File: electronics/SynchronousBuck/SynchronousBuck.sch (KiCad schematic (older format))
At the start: 58 parts, among them J101 Conn_01x02, J102 Conn_01x04_Male, J103 Conn_01x02, J104 Conn_01x02, Q101 BSC070N10NS5, Q102 BSC067N06LS3G, U101 LM5116MH

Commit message: Updated layout and schematic. Added zener diodes to protect output of measurements
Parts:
- removed R102, R109, R110: 1k2, Resistor_SMD:R_0603_1608Metric, symbol Device:R_Small
- added D102, D103: 5V1, Diode_SMD:D_SOD-123, symbol Device:D_Zener
- added R120: 24k, Resistor_SMD:R_0603_1608Metric, symbol Device:R_Small
- C101, C111: symbol Device:C -> Device:C_Small
- R101: value 24k -> 18k
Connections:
- net GND: now also C116.2, C117.2, C120.2, C121.2, R111.1, D102.2 (A), D103.2 (A); no longer C116.1, C117.1, C120.1, C121.1, R111.2
- net VCC: now also C120.1, C121.1, R101.2; no longer C120.2, C121.2, R101.1
- net VOUT: now also C116.1, C117.1, R120.1; no longer C116.2, C117.2
- net at U101.2 (UVLO): now also R101.1, R111.2; no longer R111.1
- net at J102.1 (Pin_1), R121.1, R123.2: now also D103.1 (K), R120.2
- net at J102.4 (Pin_4), R117.2, R118.1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: now also D102.1 (K)
- no-connect marks 1 -> 0
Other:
- note added: "Ethernet over power connection"
- note added: "Vin 20-50V"
- note added: "Vout set 14.5V\n"
- note removed: "Vin 30-50V"
- moved on the sheet: C101, C102, C103, C104, C105, C106, C107, C108, C109, C110, C111, C112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

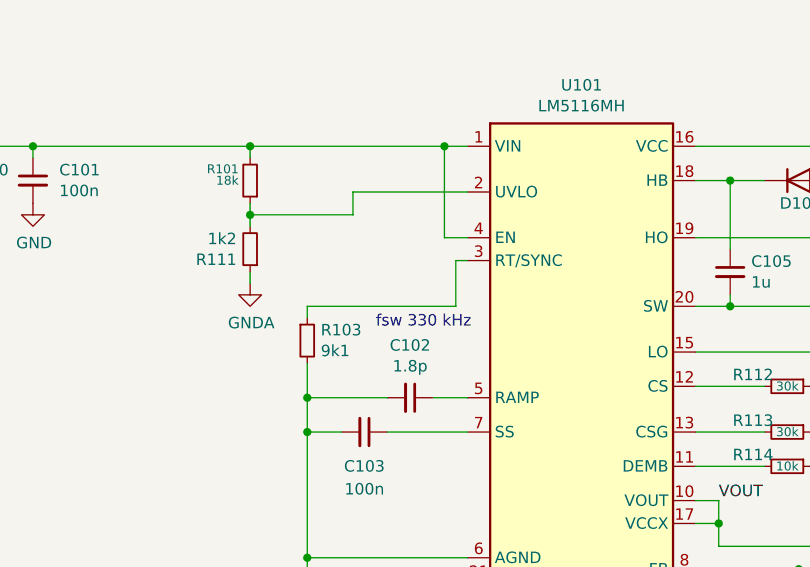
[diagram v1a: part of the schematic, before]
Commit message: BOM optimization for JLCPcb assembly
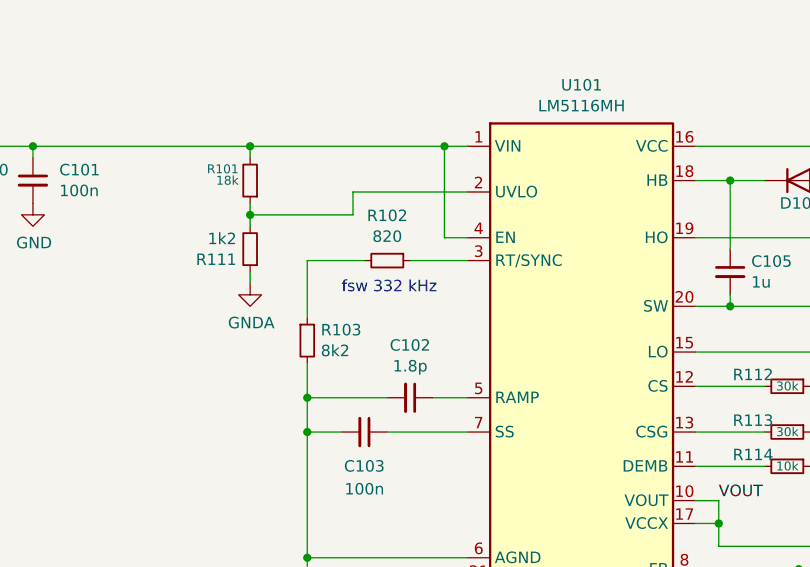
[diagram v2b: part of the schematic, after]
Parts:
- added R102: 820, Resistor_SMD:R_0603_1608Metric, symbol Device:R_Small
- C110: Config (none) -> -prod
- C116, C120, C121: Config -prod -> (none)
- R103: value 9k1 -> 8k2
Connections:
- net at U101.3 (RT/SYNC): now also R102.1; no longer R103.1
- new net: R102.2, R103.1
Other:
- note added: "fsw 332 kHz"
- note removed: "fsw 330 kHz"
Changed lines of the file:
@@
 P 6250 4150
 F 0 "R103" H 6309 4196 50  0000 L CNN
-F 1 "9k1" H 6309 4105 50  0000 L CNN
+F 1 "8k2" H 6309 4105 50  0000 L CNN
 F 2 "Resistor_SMD:R_0603_1608Metric" H 6250 4150 50  0001 C CNN
 F 3 "~" H 6250 4150 50  0001 C CNN
@@
 	1    0    0    -1
 $EndComp
-Text Notes 6550 4100 0    50   ~ 0
-fsw 330 kHz
+Text Notes 6400 3950 0    50   ~ 0
+fsw 332 kHz
 Text Notes 3550 3250 0    50   ~ 0
 Vin 20-50V
@@
 F 4 "100 V" H 12650 4150 50  0001 C CNN "Voltage"
 F 5 "C153036" H 12650 4150 50  0001 C CNN "LCSC Pn"
-F 6 "-prod" H 12650 4150 50  0001 C CNN "Config"
 	1    12650 4150
 	1    0    0    -1
@@
 F 4 "C134220" H 13400 4150 50  0001 C CNN "LCSC Pn"
 F 5 "35" H 13400 4150 50  0001 C CNN "Voltage"
+F 6 "-prod" H 13400 4150 50  0001 C CNN "Config"
 	1    13400 4150
 	1    0    0    -1
@@
 F 4 "100 V" H 4650 3450 50  0001 C CNN "Voltage"
 F 5 "C153036" H 4650 3450 50  0001 C CNN "LCSC Pn"
-F 6 "-prod" H 4650 3450 50  0001 C CNN "Config"
 	1    4650 3450
 	1    0    0    -1
@@
 F 4 "100 V" H 4250 3450 50  0001 C CNN "Voltage"
 F 5 "C153036" H 4250 3450 50  0001 C CNN "LCSC Pn"
-F 6 "-prod" H 4250 3450 50  0001 C CNN "Config"
 	1    4250 3450
 	1    0    0    -1
@@
 $EndComp
 Wire Wire Line
-	6250 4050 6250 4000
-Wire Wire Line
-	6250 4000 6900 4000
-Wire Wire Line
-	6900 4000 6900 3800
-Wire Wire Line
-	6900 3800 6950 3800
-Wire Wire Line
 	15600 4000 15350 4000
 Connection ~ 15350 4000
@@
 	0    1    1    0
 $EndComp
+$Comp
+L Device:R_Small R102
+U 1 1 60C0F9EF
+P 6600 3800
+F 0 "R102" V 6404 3800 50  0000 C CNN
+F 1 "820" V 6495 3800 50  0000 C CNN
+F 2 "Resistor_SMD:R_0603_1608Metric" H 6600 3800 50  0001 C CNN
+F 3 "~" H 6600 3800 50  0001 C CNN
+	1    6600 3800
+	0    1    1    0
+$EndComp
+Wire Wire Line
+	6500 3800 6250 3800
+Wire Wire Line
+	6250 3800 6250 4050
+Wire Wire Line
+	6700 3800 6950 3800
 $EndSCHEMATC

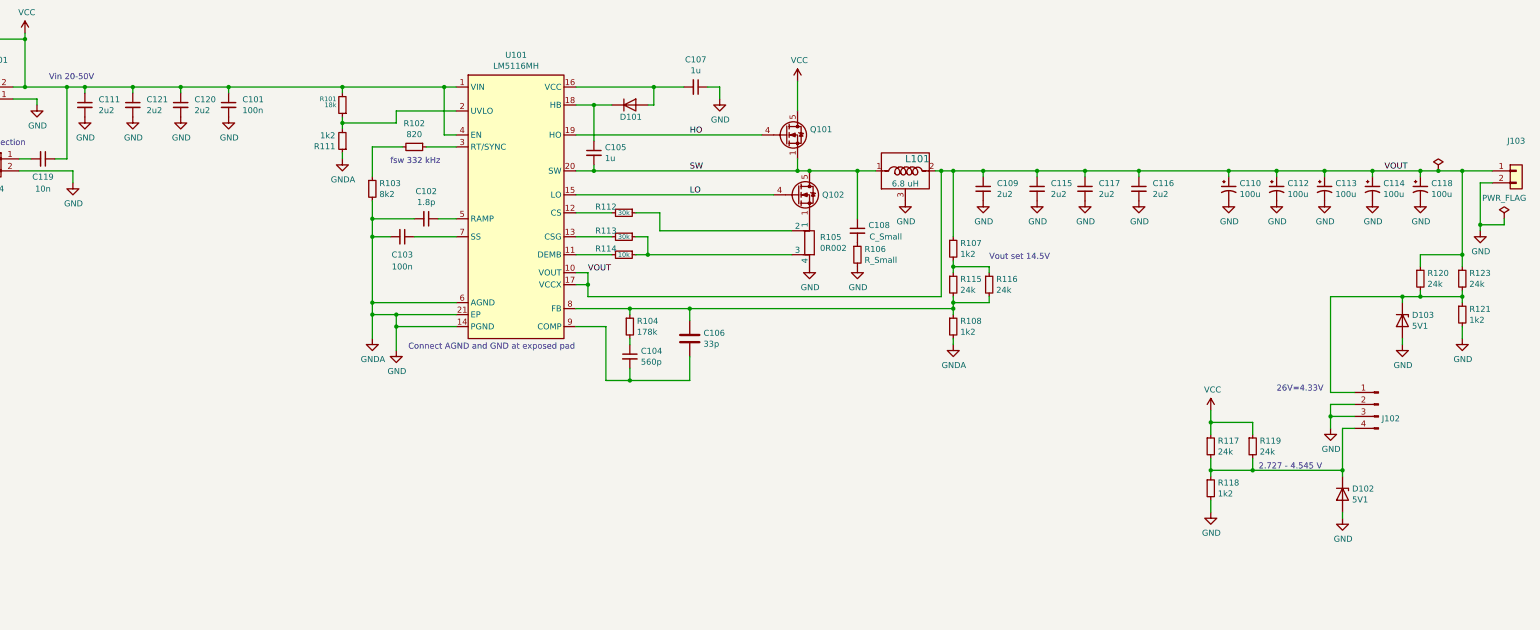
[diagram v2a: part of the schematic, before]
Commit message: Added Raspi Adapter Changed Buck Capacitors
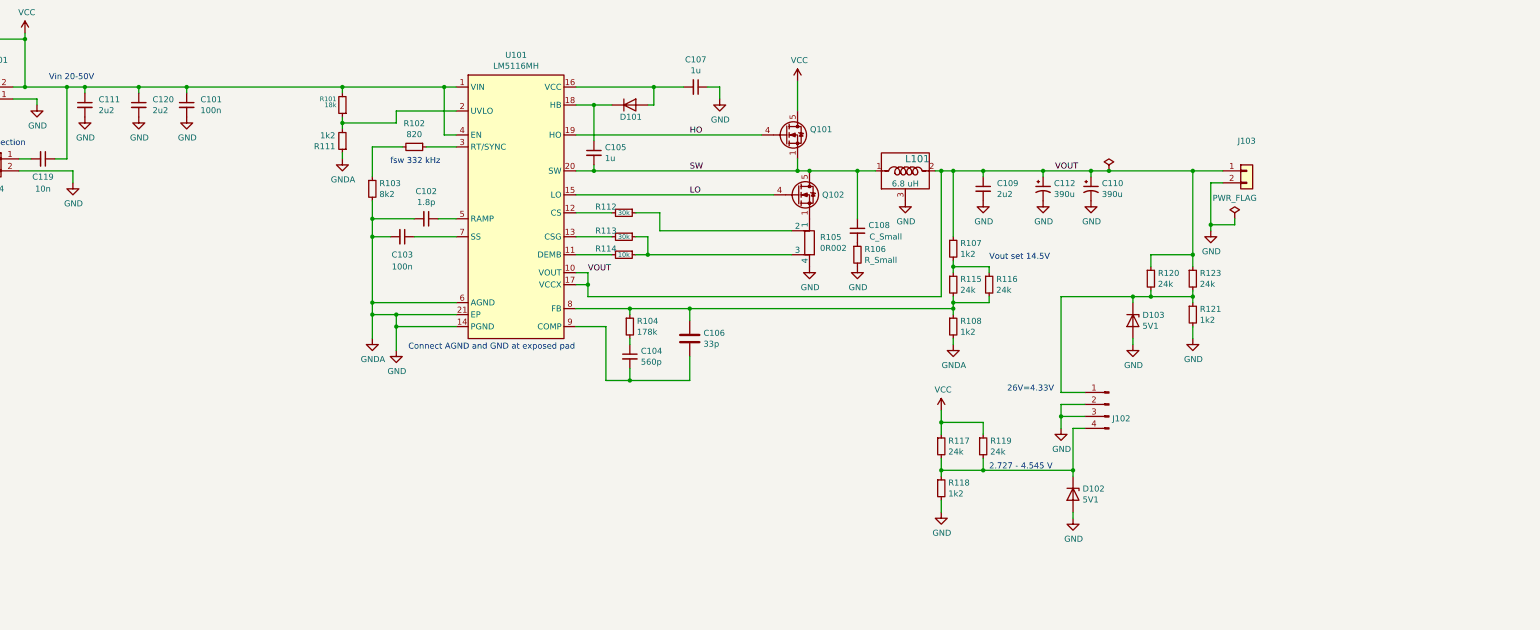
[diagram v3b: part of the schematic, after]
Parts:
- removed C113, C114, C118: 100u, Capacitor_SMD:CP_Elec_8x10, symbol Device:CP1_Small
- removed C115, C116, C117, C121: 2u2, Capacitor_SMD:C_1210_3225Metric, symbol Device:C_Small
- C110: value 100u -> 390u; footprint Capacitor_SMD:CP_Elec_6.3x7.7 -> Capacitor_SMD:CP_Elec_8x11.9; LCSC Pn C134220 -> (none); Manufacturer (none) -> Panasonic; Manufacturer Pn (none) -> 20SVPF390M; Voltage 35 -> 20V
- C112: value 100u -> 390u; footprint Capacitor_SMD:CP_Elec_8x10 -> Capacitor_SMD:CP_Elec_8x11.9; Config (none) -> -prod; LCSC Pn C487360 -> (none); Manufacturer (none) -> Panasonic; Manufacturer Pn (none) -> 20SVPF390M; Voltage 50V -> 20V
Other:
- moved on the sheet: C101, C120, D102, D103, J102, J103, R117, R118, R119, R120, R121, R123

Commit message: Updated BOM
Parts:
- C119: Config -prod -> (none)
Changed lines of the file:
@@
 F 3 "~" H 3500 3900 50  0001 C CNN
 F 4 "C57112" V 3500 3900 50  0001 C CNN "LCSC Pn"
-F 5 "-prod" V 3500 3900 50  0001 C CNN "Config"
 	1    3500 3900
 	0    1    -1   0

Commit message: Cramp value fix Updated schematic PDF
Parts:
- C102: value 1.8p -> 1n8; LCSC Pn C140677 -> C107024
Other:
- note added: "UVLO 19,44V"
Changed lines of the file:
@@
 P 6700 4400
 F 0 "C102" V 6471 4400 50  0000 C CNN
-F 1 "1.8p" V 6562 4400 50  0000 C CNN
+F 1 "1n8" V 6562 4400 50  0000 C CNN
 F 2 "Capacitor_SMD:C_0402_1005Metric" H 6700 4400 50  0001 C CNN
 F 3 "~" H 6700 4400 50  0001 C CNN
-F 4 "C140677" V 6700 4400 50  0001 C CNN "LCSC Pn"
+F 4 "C107024" V 6700 4400 50  0001 C CNN "LCSC Pn"
 	1    6700 4400
 	0    1    1    0
@@
 Wire Wire Line
 	3850 3300 4300 3300
+Text Notes 5450 3600 0    50   ~ 0
+UVLO 19,44V
 $EndSCHEMATC

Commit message: Production Commit
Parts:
- added C113, C114: C_Small, Capacitor_SMD:C_0603_1608Metric, symbol Device:C_Small
- C102: value 1n8 -> 680p; LCSC Pn C107024 -> C307451
- R105: value 0R002 -> 0R005; footprint PCBDecals:R_2512_6332Metric_SHUNT -> PCBDecals:LR2512_3WLOW_SHUNT; LCSC Pn C457118 -> C154688
- R112, R113: value 30k -> 100
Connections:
- net GND: now also C113.2
- net VOUT: now also C114.1
- net at C106.1, R104.1, R108.1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: now also C113.1, C114.2
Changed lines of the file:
@@
 L power:GNDA #PWR0108
 U 1 1 60BC6C9E
-P 11100 5450
-F 0 "#PWR0108" H 11100 5200 50  0001 C CNN
-F 1 "GNDA" H 11105 5277 50  0000 C CNN
-F 2 "" H 11100 5450 50  0001 C CNN
-F 3 "" H 11100 5450 50  0001 C CNN
-	1    11100 5450
+P 11100 5500
+F 0 "#PWR0108" H 11100 5250 50  0001 C CNN
+F 1 "GNDA" H 11105 5327 50  0000 C CNN
+F 2 "" H 11100 5500 50  0001 C CNN
+F 3 "" H 11100 5500 50  0001 C CNN
+	1    11100 5500
 	1    0    0    -1
 $EndComp
@@
 P 6700 4400
 F 0 "C102" V 6471 4400 50  0000 C CNN
-F 1 "1n8" V 6562 4400 50  0000 C CNN
+F 1 "680p" V 6562 4400 50  0000 C CNN
 F 2 "Capacitor_SMD:C_0402_1005Metric" H 6700 4400 50  0001 C CNN
 F 3 "~" H 6700 4400 50  0001 C CNN
-F 4 "C107024" V 6700 4400 50  0001 C CNN "LCSC Pn"
+F 4 "C307451" V 6700 4400 50  0001 C CNN "LCSC Pn"
 	1    6700 4400
 	0    1    1    0
@@
 P 8350 4550
 F 0 "R113" V 8300 4400 50  0000 C CNN
-F 1 "30k" V 8350 4550 39  0000 C CNN
+F 1 "100" V 8350 4550 39  0000 C CNN
 F 2 "Resistor_SMD:R_0603_1608Metric" H 8350 4550 50  0001 C CNN
 F 3 "~" H 8350 4550 50  0001 C CNN
@@
 P 8350 4350
 F 0 "R112" V 8300 4200 50  0000 C CNN
-F 1 "30k" V 8350 4350 39  0000 C CNN
+F 1 "100" V 8350 4350 39  0000 C CNN
 F 2 "Resistor_SMD:R_0603_1608Metric" H 8350 4350 50  0001 C CNN
 F 3 "~" H 8350 4350 50  0001 C CNN
@@
 P 9900 4600
 F 0 "R105" H 9812 4646 50  0000 R CNN
-F 1 "0R002" H 9812 4555 50  0000 R CNN
-F 2 "PCBDecals:R_2512_6332Metric_SHUNT" V 9830 4600 50  0001 C CNN
+F 1 "0R005" H 9812 4555 50  0000 R CNN
+F 2 "PCBDecals:LR2512_3WLOW_SHUNT" V 9830 4600 50  0001 C CNN
 F 3 "~" H 9900 4600 50  0001 C CNN
-F 4 "C457118" H 9900 4600 50  0001 C CNN "LCSC Pn"
+F 4 "C154688" H 9900 4600 50  0001 C CNN "LCSC Pn"
 	1    9900 4600
 	-1   0    0    -1
@@
 	11100 4750 11100 4800
 Wire Wire Line
-	11100 4000 11100 4550
+	11100 4000 11100 4500
 Wire Wire Line
 	11100 4800 11400 4800
@@
 Text Notes 5450 3600 0    50   ~ 0
 UVLO 19,44V
+$Comp
+L Device:C_Small C113
+U 1 1 60C9AF9C
+P 11500 5300
+F 0 "C113" H 11592 5346 50  0000 L CNN
+F 1 "C_Small" H 11600 5250 50  0000 L CNN
+F 2 "Capacitor_SMD:C_0603_1608Metric" H 11500 5300 50  0001 C CNN
+F 3 "~" H 11500 5300 50  0001 C CNN
+F 4 "-prod" H 11500 5300 50  0001 C CNN "Config"
+	1    11500 5300
+	1    0    0    -1
+$EndComp
+$Comp
+L Device:C_Small C114
+U 1 1 60C9D375
+P 11750 4950
+F 0 "C114" H 11842 4996 50  0000 L CNN
+F 1 "C_Small" H 11850 4900 50  0000 L CNN
+F 2 "Capacitor_SMD:C_0603_1608Metric" H 11750 4950 50  0001 C CNN
+F 3 "~" H 11750 4950 50  0001 C CNN
+F 4 "-prod" H 11750 4950 50  0001 C CNN "Config"
+	1    11750 4950
+	1    0    0    -1
+$EndComp
+Wire Wire Line
+	11750 4850 11750 4500
+Wire Wire Line
+	11750 4500 11100 4500
+Connection ~ 11100 4500
+Wire Wire Line
+	11100 4500 11100 4550
+Wire Wire Line
+	11750 5050 11750 5100
+Wire Wire Line
+	11750 5100 11500 5100
+Connection ~ 11400 5100
+Wire Wire Line
+	11500 5200 11500 5100
+Connection ~ 11500 5100
+Wire Wire Line
+	11500 5100 11400 5100
+Wire Wire Line
+	11100 5450 11500 5450
+Wire Wire Line
+	11500 5450 11500 5400
+Connection ~ 11100 5450
+Wire Wire Line
+	11100 5450 11100 5500
 $EndSCHEMATC
